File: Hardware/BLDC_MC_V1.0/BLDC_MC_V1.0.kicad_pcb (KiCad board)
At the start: 8 copper layers, 120 x 55 mm, 229 parts, among them J1 Conn_01x01_Pin, J2 Conn_01x01_Pin, J3 USB_C_Receptacle_USB2.0_16P, J4 Conn_02x03_Counter_Clockwise, J5 S6B-PH-K-S_LF__SN_, J6 Conn_01x01_Pin, J7 Conn_01x01_Pin, J8 S10B-PHDSS LFSN, J9 Conn_01x01_Pin, Q1 BSC027N10NS5ATMA1, Q2 BSC027N10NS5ATMA1, Q3 BSC027N10NS5ATMA1, Q4 BSC027N10NS5ATMA1, Q5 BSC027N10NS5ATMA1, Q6 BSC027N10NS5ATMA1, Q7 BSC027N10NS5ATMA1, SW1 SW_Push, U1 LM76005RNPR, U10 TLV9061IDBVR, U11 TLV9061IDBVR, U12 TLV9061IDBVR, U13 TLV9061IDBVR, U14 TLV9061IDBVR, U15 TLV9061IDBVR, U16 LM74700QDRQ1, U2 TCAN334DR, U3 TLV9061IDBVR, U4 STM32G431RBT6, U5 LDL1117S33R, U6 DRV8353HRTAR, U7 NCV4274ADT50RKG, U8 25LC256-E_SN, U9 USBLC6-2SC6, Y1 7M-24.000MAAJ-T, Y2 ABS07-32.768KHZ-T

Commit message: Update board layout
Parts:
- moved C78 3.05 mm to (128.6, 61.2)
- moved C80 3.05 mm to (128.8, 44.5)
- moved C82 3.05 mm to (128.6, 29.2)
- moved NT1 3.05 mm to (138.4, 59.1)
- moved NT2 3.05 mm to (138.4, 42.2)
- moved NT3 3.05 mm to (138.4, 25.9)
- moved Q4 3.05 mm to (127.5, 21.1)
- moved Q5 3.05 mm to (127.1, 36.7)
- moved Q6 3.05 mm to (127.0, 53.5)
- moved R71 3.05 mm to (135.0, 35.6)
- moved R74 3.05 mm to (135.8, 19.9)
- moved R22 3.05 mm to (134.4, 60.3)
- moved R7 3.05 mm to (135.1, 52.5)
- moved R73 3.05 mm to (134.4, 42.5)
- moved R76 3.05 mm to (134.4, 26.5)
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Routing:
- net +3.3V: track 155.6 -> 181.3 mm, vias 23 -> 21
- net /BLDC_MC_V1.0_MCU/MISO: track 21.3 -> 25.1 mm
- net Net-(R55-Pad2): track 4.09 -> 5.68 mm
- net /BLDC_MC_V1.0_Connectors/Hall_B: track 62.4 -> 61.0 mm
- net Net-(R58-Pad2): track 4.34 -> 5.71 mm
- net GND: track 189.0 -> 190.3 mm, vias 41 -> 42
- net Net-(R61-Pad2): track 4.27 -> 5.40 mm
- net /BLDC_MC_V1.0_CAN_Transceiver/CAN_STB: track 32.9 -> 32.1 mm
- net /BLDC_MC_V1.0_CAN_Transceiver/CAN_SHDN: track 39.1 -> 39.6 mm
- net Vin: vias 10 -> 23
- added copper zone on In3.Cu, net Vin
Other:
- board size 120 x 55 mm -> 118.8 x 55 mm

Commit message: Update the board layout
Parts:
- moved R8 0.14 mm to (118.2, 58.6)
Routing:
- net Net-(C77-Pad2): track 0.00 -> 4.12 mm
- net Net-(C81-Pad2): track 0.00 -> 4.04 mm
- net Net-(C79-Pad2): track 0.00 -> 3.91 mm
- net +3.3V: track 181.3 -> 184.5 mm
- net /BLDC_MC_V1.0_CAN_Transceiver/IC_TXD: track 54.4 -> 52.7 mm
- net /BLDC_MC_V1.0_Memory/CS: track 17.9 -> 17.3 mm
- net /BLDC_MC_V1.0_Connectors/Vin_DC: vias 32 -> 30

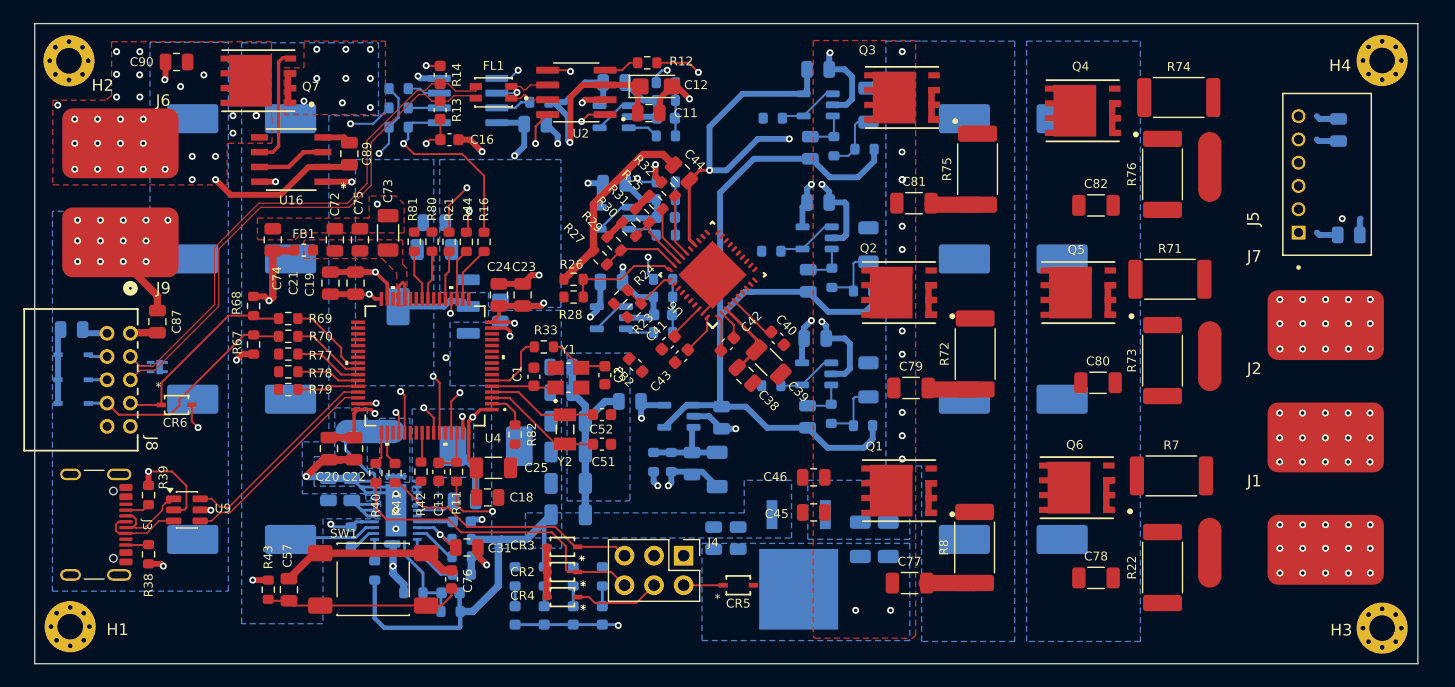
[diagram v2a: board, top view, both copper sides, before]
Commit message: Routing the power connections and some GD signals
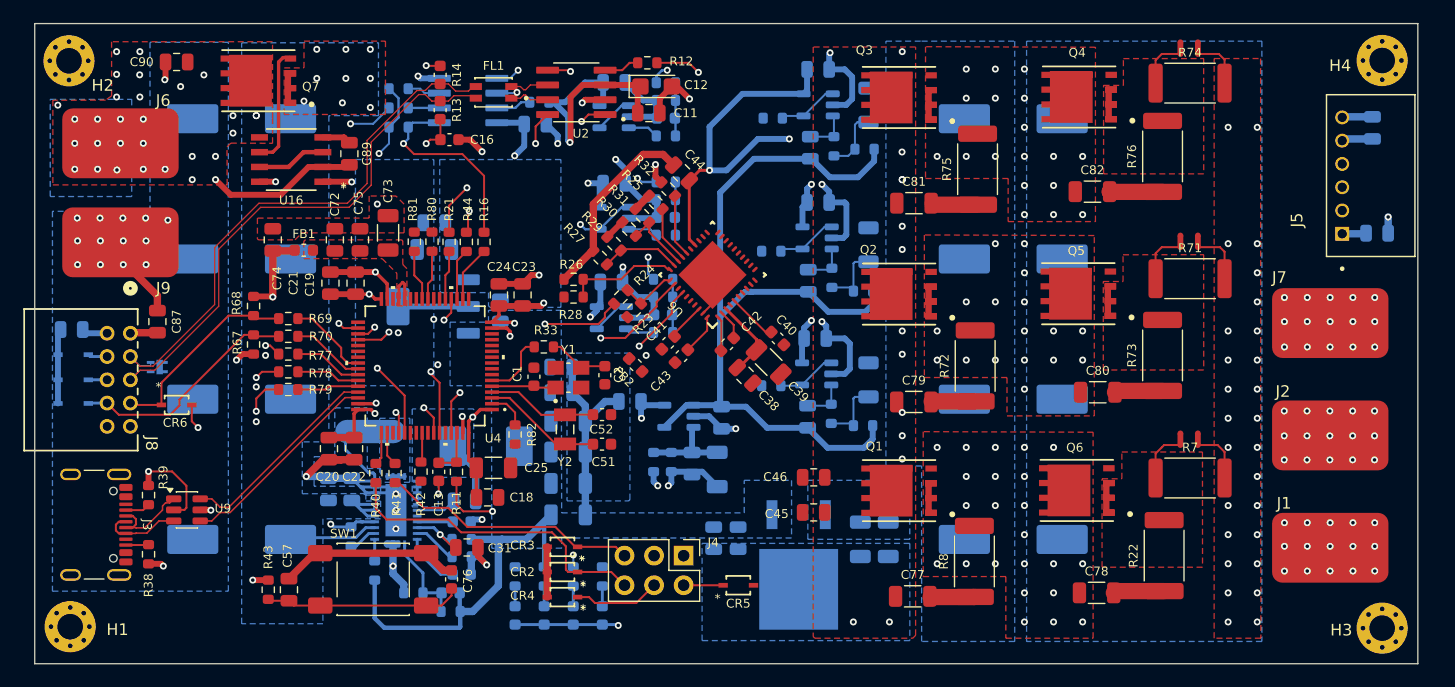
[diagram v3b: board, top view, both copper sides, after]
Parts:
- removed NT1, NT2, NT3: NetTie_2, NetTie:NetTie-2_SMD_Pad2.0mm
- added NT10: NetTie_2, NetTie:NetTie-2_SMD_Pad0.5mm, F.Cu at (137.4, 15.7)
- added NT5: NetTie_2, NetTie:NetTie-2_SMD_Pad0.5mm, F.Cu at (135.9, 32.3)
- added NT6: NetTie_2, NetTie:NetTie-2_SMD_Pad0.5mm, F.Cu at (137.4, 32.3)
- added NT7: NetTie_2, NetTie:NetTie-2_SMD_Pad0.5mm, F.Cu at (135.9, 49.3)
- added NT8: NetTie_2, NetTie:NetTie-2_SMD_Pad0.5mm, F.Cu at (137.4, 49.3)
- added NT9: NetTie_2, NetTie:NetTie-2_SMD_Pad0.5mm, F.Cu at (135.9, 15.7)
- moved J5 3.75 mm to (152.2, 26.6)
- moved C64 2.93 mm to (152.4, 22.6)
- moved C65 2.44 mm to (152.8, 31.6)
- moved R71 1.73 mm to (136.7, 35.5)
- moved R7 1.62 mm to (136.7, 52.6)
- moved R74 1.57 mm to (136.7, 18.7)
- moved R76 1.54 mm to (134.4, 25.0)
- moved C78 1.29 mm to (128.7, 62.5)
- moved C79 1.23 mm to (113.0, 46.1)
- moved C82 1.22 mm to (128.3, 28.0)
- moved Q4 1.22 mm to (127.2, 19.9)
- moved R8 1.20 mm to (118.2, 59.8)
- moved C77 1.17 mm to (112.9, 62.8)
- moved R22 1.03 mm to (134.5, 59.3)
- moved R72 1.02 mm to (118.3, 43.0)
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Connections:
- C11 pad 1: +3.3V -> GND
- C12 pad 1: +3.3V -> GND
- C13 pad 1: +3.3V -> GND
- C17 pad 1: +3.3V -> GND
- C18 pad 1: +3.3V -> GND
- C19 pad 1: +3.3V -> GND
- C20 pad 1: +3.3V -> GND
- C21 pad 1: +3.3V -> GND
- C22 pad 1: +3.3V -> GND
- C23 pad 1: +3.3V -> GND
- C24 pad 1: +3.3V -> GND
- C25 pad 1: +3.3V -> GND
- C44 pad 1: +3.3V -> GND
- C61 pad 1: +3.3V -> GND
- C62 pad 1: +3.3V -> GND
- C63 pad 1: +3.3V -> GND
- C64 pad 1: +3.3V -> GND
- C74 pad 1: +3.3V -> GND
- C83 pad 1: +3.3V -> GND
- C84 pad 1: +3.3V -> GND
- C85 pad 1: +3.3V -> GND
- C86 pad 1: +3.3V -> GND
- C87 pad 1: +3.3V -> GND
- FB1 pad 2: +3.3V -> GND
- J5 pad 5: +3.3V -> GND
- J8 pad 1: +3.3V -> GND
- Q4 pad 1: /BLDC_MC_V1.0_Gate_Drive/SC+ -> Net-(NT9-Pad2)
- Q4 pad 2: /BLDC_MC_V1.0_Gate_Drive/SC+ -> Net-(NT9-Pad2)
- Q4 pad 3: /BLDC_MC_V1.0_Gate_Drive/SC+ -> Net-(NT9-Pad2)
- Q5 pad 1: /BLDC_MC_V1.0_Gate_Drive/SB+ -> Net-(NT5-Pad2)
- Q5 pad 2: /BLDC_MC_V1.0_Gate_Drive/SB+ -> Net-(NT5-Pad2)
- Q5 pad 3: /BLDC_MC_V1.0_Gate_Drive/SB+ -> Net-(NT5-Pad2)
- Q6 pad 1: /BLDC_MC_V1.0_Gate_Drive/SA+ -> Net-(NT7-Pad2)
- Q6 pad 2: /BLDC_MC_V1.0_Gate_Drive/SA+ -> Net-(NT7-Pad2)
- Q6 pad 3: /BLDC_MC_V1.0_Gate_Drive/SA+ -> Net-(NT7-Pad2)
- R17 pad 2: +3.3V -> GND
- R18 pad 2: +3.3V -> GND
- R19 pad 2: +3.3V -> GND
- R22 pad 2: /BLDC_MC_V1.0_Gate_Drive/SA+ -> Net-(NT7-Pad2)
- R32 pad 1: +3.3V -> GND
- R36 pad 1: +3.3V -> GND
- R43 pad 2: +3.3V -> GND
- R53 pad 2: +3.3V -> GND
- R67 pad 2: +3.3V -> GND
- R68 pad 2: +3.3V -> GND
- R7 pad 1: /BLDC_MC_V1.0_Gate_Drive/SA+ -> Net-(NT7-Pad2)
- R7 pad 2: /BLDC_MC_V1.0_Gate_Drive/SA- -> GND
- R71 pad 1: /BLDC_MC_V1.0_Gate_Drive/SB+ -> Net-(NT5-Pad2)
- R71 pad 2: /BLDC_MC_V1.0_Gate_Drive/SB- -> GND
- R73 pad 2: /BLDC_MC_V1.0_Gate_Drive/SB+ -> Net-(NT5-Pad2)
- R74 pad 1: /BLDC_MC_V1.0_Gate_Drive/SC+ -> Net-(NT9-Pad2)
- R74 pad 2: /BLDC_MC_V1.0_Gate_Drive/SC- -> GND
- R76 pad 2: /BLDC_MC_V1.0_Gate_Drive/SC+ -> Net-(NT9-Pad2)
- U10 pad 5: +3.3V -> GND
- U11 pad 5: +3.3V -> GND
- U12 pad 5: +3.3V -> GND
- U13 pad 5: +3.3V -> GND
- U14 pad 5: +3.3V -> GND
- U15 pad 5: +3.3V -> GND
- U2 pad 3: +3.3V -> GND
- U3 pad 5: +3.3V -> GND
- U4 pad 1: +3.3V -> GND
- U4 pad 16: +3.3V -> GND
- U4 pad 32: +3.3V -> GND
- U4 pad 48: +3.3V -> GND
- U4 pad 64: +3.3V -> GND
- U5 pad 2: +3.3V -> GND
- U5 pad 4: +3.3V -> GND
- U6 pad 24: +3.3V -> GND
- U8 pad 8: +3.3V -> GND
- U9 pad 5: +3.3V -> GND
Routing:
- net GND: track 190.3 -> 396.2 mm, vias 42 -> 98
- net +3.3V: track 184.5 -> 0.00 mm, vias 21 -> 0
- net /BLDC_MC_V1.0_Gate_Drive/PWM_B_H: track 0.00 -> 42.6 mm, vias 0 -> 2
- net /BLDC_MC_V1.0_Gate_Drive/PWM_A_H: track 0.00 -> 39.4 mm, vias 0 -> 2
- net /BLDC_MC_V1.0_Gate_Drive/PWM_C_H: track 0.00 -> 39.2 mm, vias 0 -> 2
- net /BLDC_MC_V1.0_Gate_Drive/GD_Enable: track 0.00 -> 27.9 mm, vias 0 -> 2
- net /BLDC_MC_V1.0_HallSensor/Hall_Phase_B: track 3.30 -> 28.6 mm, vias 0 -> 2
- net Net-(C82-Pad2): track 0.00 -> 4.56 mm
- net Net-(NT7-Pad2): track 0.00 -> 4.54 mm
- net Net-(NT5-Pad2): track 0.00 -> 4.53 mm
- net Net-(C78-Pad2): track 0.00 -> 4.39 mm
- net Net-(NT9-Pad2): track 0.00 -> 4.33 mm
- net Net-(C80-Pad2): track 0.00 -> 4.14 mm
- net /BLDC_MC_V1.0_Connectors/Hall_C: track 60.8 -> 63.7 mm
- net /BLDC_MC_V1.0_Connectors/Hall_B: track 60.9 -> 63.1 mm
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- added copper zone on F.Cu, net /BLDC_MC_V1.0_3Phase_Inverter_legs/Phase_A
- added copper zone on In2.Cu, net /BLDC_MC_V1.0_3Phase_Inverter_legs/Phase_A
- added copper zone on In3.Cu, net /BLDC_MC_V1.0_3Phase_Inverter_legs/Phase_A
- added copper zone on F.Cu, net /BLDC_MC_V1.0_3Phase_Inverter_legs/Phase_B
- added copper zone on In2.Cu, net /BLDC_MC_V1.0_3Phase_Inverter_legs/Phase_B
- added copper zone on In3.Cu, net /BLDC_MC_V1.0_3Phase_Inverter_legs/Phase_B
- added copper zone on F.Cu, net /BLDC_MC_V1.0_3Phase_Inverter_legs/Phase_C
- added copper zone on In2.Cu, net /BLDC_MC_V1.0_3Phase_Inverter_legs/Phase_C
- added copper zone on In3.Cu, net /BLDC_MC_V1.0_3Phase_Inverter_legs/Phase_C
- added copper zone on B.Cu, net /BLDC_MC_V1.0_Connectors/Vin_DC
- added copper zone on F.Cu, net Net-(NT5-Pad2)
- added copper zone on F.Cu, net Net-(NT7-Pad2)
- added copper zone on F.Cu, net Net-(NT9-Pad2)

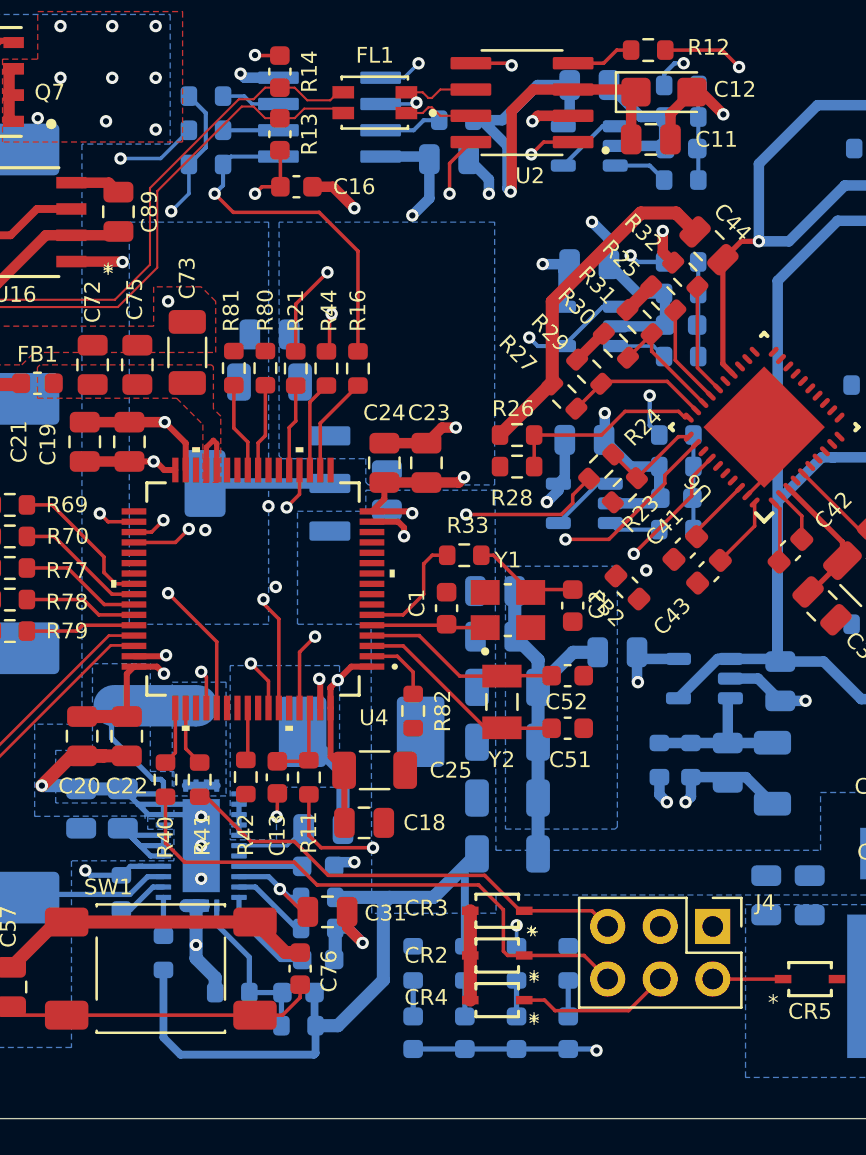
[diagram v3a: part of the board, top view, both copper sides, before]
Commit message: Update the layout and routing of the board by connecting some of the gate driver traces
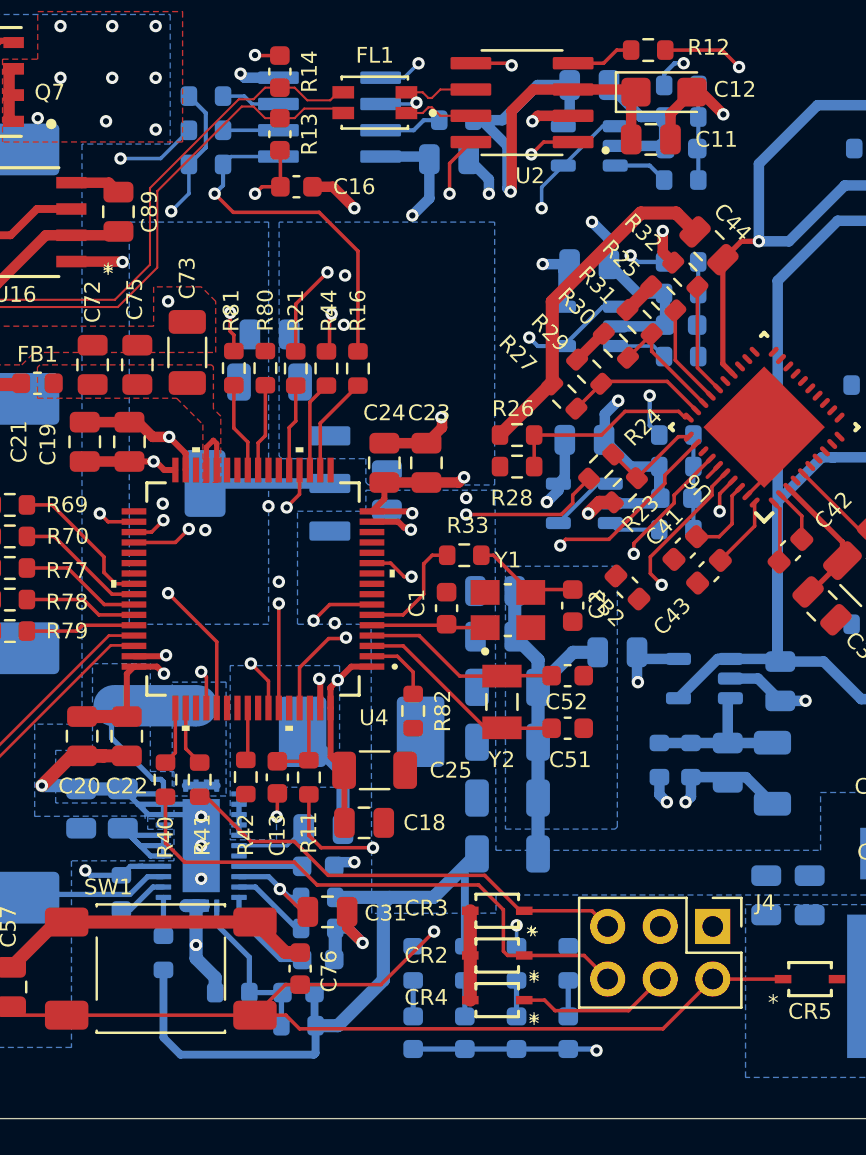
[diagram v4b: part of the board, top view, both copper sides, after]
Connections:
- C11 pad 1: GND -> +3.3V
- C12 pad 1: GND -> +3.3V
- C13 pad 1: GND -> +3.3V
- C17 pad 1: GND -> +3.3V
- C18 pad 1: GND -> +3.3V
- C19 pad 1: GND -> +3.3V
- C20 pad 1: GND -> +3.3V
- C21 pad 1: GND -> +3.3V
- C22 pad 1: GND -> +3.3V
- C23 pad 1: GND -> +3.3V
- C24 pad 1: GND -> +3.3V
- C25 pad 1: GND -> +3.3V
- C44 pad 1: GND -> +3.3V
- C61 pad 1: GND -> +3.3V
- C62 pad 1: GND -> +3.3V
- C63 pad 1: GND -> +3.3V
- C64 pad 1: GND -> +3.3V
- C74 pad 1: GND -> +3.3V
- C83 pad 1: GND -> +3.3V
- C84 pad 1: GND -> +3.3V
- C85 pad 1: GND -> +3.3V
- C86 pad 1: GND -> +3.3V
- C87 pad 1: GND -> +3.3V
- FB1 pad 2: GND -> +3.3V
- J5 pad 5: GND -> +3.3V
- J8 pad 1: GND -> +3.3V
- R17 pad 2: GND -> +3.3V
- R18 pad 2: GND -> +3.3V
- R19 pad 2: GND -> +3.3V
- R32 pad 1: GND -> +3.3V
- R36 pad 1: GND -> +3.3V
- R43 pad 2: GND -> +3.3V
- R53 pad 2: GND -> +3.3V
- R67 pad 2: GND -> +3.3V
- R68 pad 2: GND -> +3.3V
- U10 pad 5: GND -> +3.3V
- U11 pad 5: GND -> +3.3V
- U12 pad 5: GND -> +3.3V
- U13 pad 5: GND -> +3.3V
- U14 pad 5: GND -> +3.3V
- U15 pad 5: GND -> +3.3V
- U2 pad 3: GND -> +3.3V
- U3 pad 5: GND -> +3.3V
- U4 pad 1: GND -> +3.3V
- U4 pad 16: GND -> +3.3V
- U4 pad 32: GND -> +3.3V
- U4 pad 48: GND -> +3.3V
- U4 pad 64: GND -> +3.3V
- U5 pad 2: GND -> +3.3V
- U5 pad 4: GND -> +3.3V
- U6 pad 24: GND -> +3.3V
- U8 pad 8: GND -> +3.3V
- U9 pad 5: GND -> +3.3V
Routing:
- net +3.3V: track 0.00 -> 190.4 mm, vias 0 -> 24
- net GND: track 396.2 -> 207.6 mm, vias 98 -> 80
- net /BLDC_MC_V1.0_MCU/NRST: track 20.2 -> 72.0 mm, vias 0 -> 2
- net /BLDC_MC_V1.0_Gate_Drive/PWM_C_L: track 0.00 -> 33.6 mm, vias 0 -> 2
- net /BLDC_MC_V1.0_HallSensor/Hall_Phase_C: track 3.30 -> 29.4 mm, vias 0 -> 2
- net /BLDC_MC_V1.0_Gate_Drive/PWM_C_H: track 39.2 -> 47.1 mm
- net /BLDC_MC_V1.0_HallSensor/Hall_Phase_B: track 28.6 -> 36.4 mm
- net /BLDC_MC_V1.0_CAN_Transceiver/CAN_SHDN: track 40.4 -> 38.4 mm
- net /BLDC_MC_V1.0_Gate_Drive/PWM_B_L: track 0.00 -> 0.76 mm
- net /BLDC_MC_V1.0_Gate_Drive/DVDD: track 5.04 -> 5.68 mm
